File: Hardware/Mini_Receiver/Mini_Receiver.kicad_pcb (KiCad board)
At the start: 2 copper layers, 25.5 x 25 mm, 13 parts, among them J1 Conn_01x10_Male, J2 Conn_01x10_Male, J3 Conn_01x10_Male, SW1 KEY, U1 STC8H1K28_LQFP32, U2 XC6206PxxxMR, U3 RF24_SMD

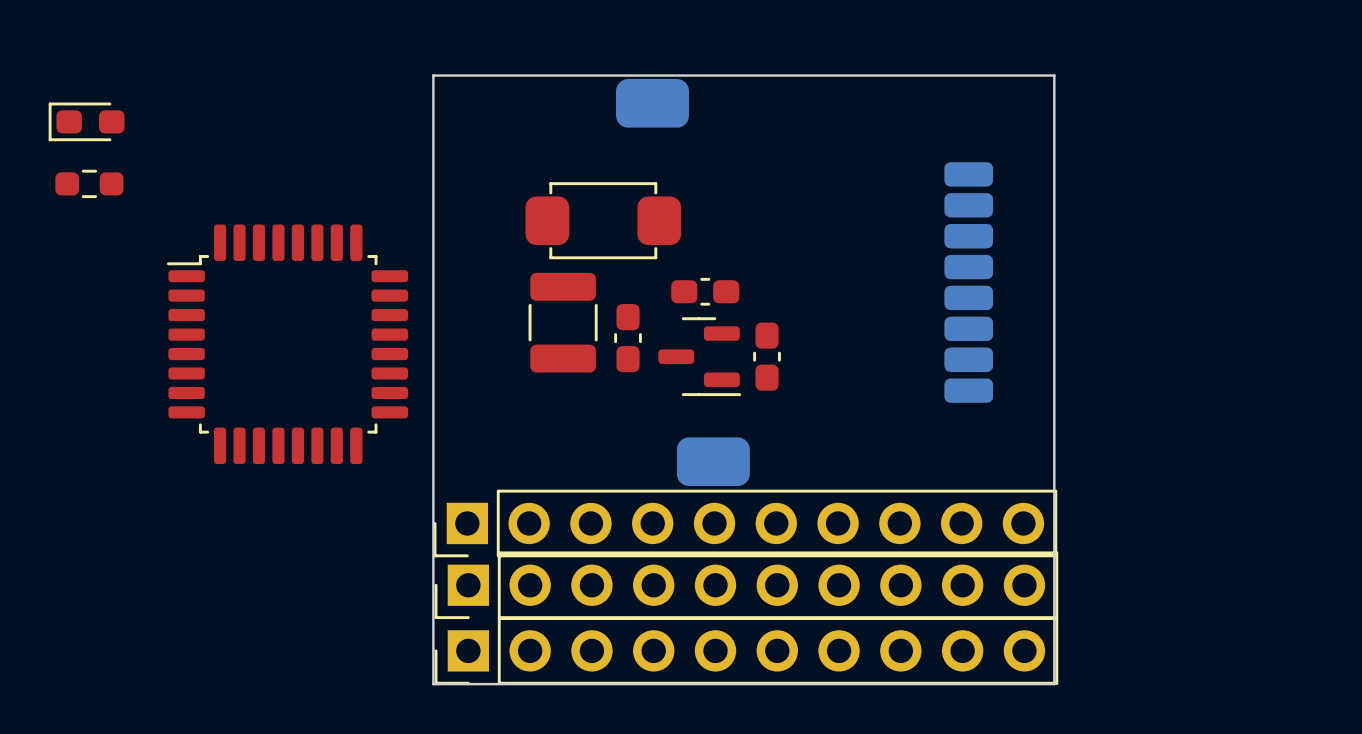
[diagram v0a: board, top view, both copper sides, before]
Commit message: 完成12通道接收机PCB初板设计并发送打样，等待验证
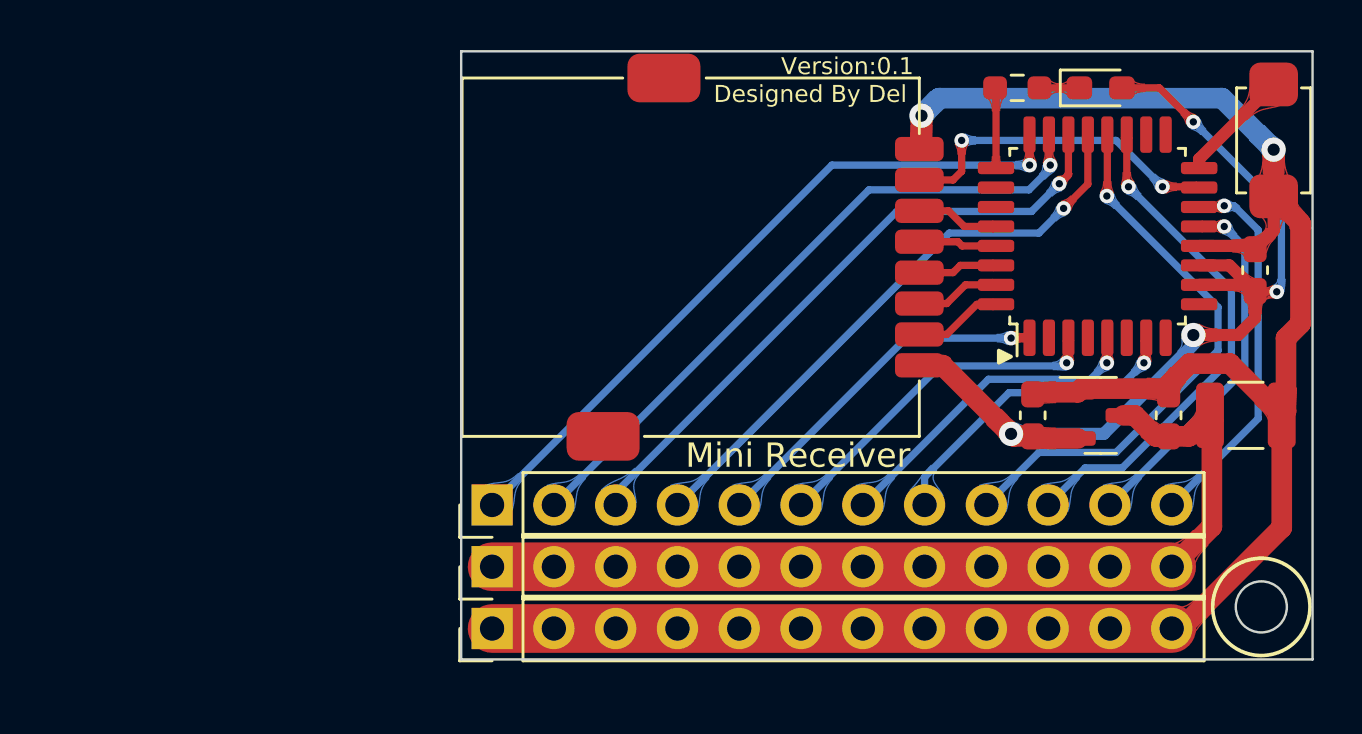
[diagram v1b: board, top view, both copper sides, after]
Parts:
- J1, J2, J3: value Conn_01x10_Male -> Conn_01x12_Male; footprint Connector_PinHeader_2.54mm:PinHeader_1x10_P2.54mm_Vertical -> Connector_PinHeader_2.54mm:PinHeader_1x12_P2.54mm_Vertical
- U3: moved to F.Cu
- moved D1 41.6 mm to (120.3, 97.2)
- moved R1 38.3 mm to (116.8, 97.2), turned to 180 degrees
- moved U1 33.6 mm to (120.1, 103.3), turned to 90 degrees
- moved C1 28.3 mm to (126.2, 110.6), turned to 0 degrees
- moved SW1 27.8 mm to (127.4, 99.3), turned to -90 degrees
- moved C2 22.5 mm to (123.1, 110.6)
- moved C4 20.4 mm to (126.6, 104.6), turned to 90 degrees
- moved U2 16.7 mm to (120.3, 110.6), turned to 0 degrees
- moved C3 14.4 mm to (117.5, 110.6), turned to 90 degrees
- moved U3 2.28 mm to (112.8, 104.1), turned to 90 degrees
- moved J3 1.34 mm to (95.2, 119.4)
- moved J1 1.27 mm to (95.2, 114.3)
- moved J2 1.24 mm to (95.2, 116.8)
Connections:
- J1 pad 1: /PWM1 -> /PWM8
- J1 pad 10: /RXD -> /CH11
- J1 pad 2: /PWM2 -> /PWM7
- J1 pad 3: /PWM3 -> /PWM6
- J1 pad 4: /PWM4 -> /PWM5
- J1 pad 5: /PWM5 -> /PWM1
- J1 pad 6: /PWM6 -> /PWM2
- J1 pad 7: /PWM7 -> /PWM3
- J1 pad 8: /PWM8 -> /PWM4
- J1 pad 9: /TXD -> /CH10
- U1 pad 16: unconnected-(U1-Pad16) -> /KEY
- U1 pad 19: unconnected-(U1-Pad19) -> /CH11
- U1 pad 20: unconnected-(U1-Pad20) -> /CH10
- U1 pad 26: /KEY -> unconnected-(U1-Pad26)
- U1 pad 28: /CE -> /MISO
- U1 pad 29: /CSN -> /MOSI
- U1 pad 31: /MOSI -> /CSN
- U1 pad 32: /MISO -> /CE
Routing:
- net GND: track 0.00 -> 84.5 mm, vias 0 -> 2
- net +3V3: track 0.00 -> 39.2 mm, vias 0 -> 4
- net VCC: track 0.00 -> 39.2 mm
- net /PWM8: track 0.00 -> 29.1 mm, vias 0 -> 1
- net /PWM7: track 0.00 -> 27.6 mm, vias 0 -> 1
- net /PWM6: track 0.00 -> 26.2 mm, vias 0 -> 1
- net /PWM5: track 0.00 -> 24.4 mm, vias 0 -> 1
- net /CH10: track 0.00 -> 22.9 mm, vias 0 -> 1
- net /CH11: track 0.00 -> 21.0 mm, vias 0 -> 1
- net /TXD: track 0.00 -> 15.6 mm, vias 0 -> 1
- net /RXD: track 0.00 -> 15.1 mm, vias 0 -> 1
- net /PWM1: track 0.00 -> 14.8 mm, vias 0 -> 1
- net /PWM2: track 0.00 -> 14.4 mm, vias 0 -> 1
- net /IRQ: track 0.00 -> 13.7 mm, vias 0 -> 2
- net /PWM3: track 0.00 -> 13.5 mm, vias 0 -> 1
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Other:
- board size 25.5 x 25 mm -> 35 x 25 mm
- board text added: "5V"
- board text added: "CH0"
- board text added: "CH1"
- board text added: "CH2"
- board text added: "CH3"
- board text added: "CH4"
- board text added: "CH5"
- board text added: "CH6"
- board text added: "CH7"
- board text added: "CH8"
- board text added: "CH9"
- board text added: "Designed By Del"
- board text added: "Mini Receiver"
- board text added: "RXD"
- board text added: "TXD"
- board text added: "Version:0.1"
